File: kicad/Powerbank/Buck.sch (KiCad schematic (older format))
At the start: 1 part

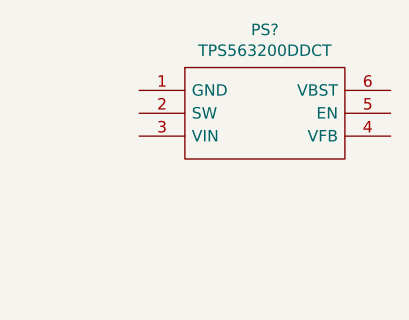
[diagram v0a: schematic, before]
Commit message: Battery charger completed according to reference guide
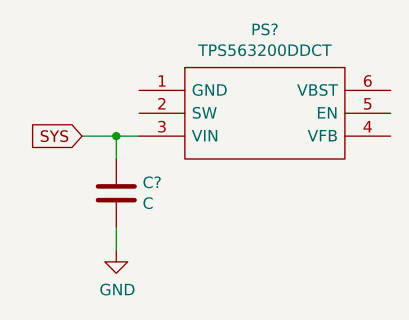
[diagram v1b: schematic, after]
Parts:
- added C?: C, symbol Device:C
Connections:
- net SYS: now reaches PS?.3 (VIN)
- net SYS: now also C?.1
- new net GND: C?.2
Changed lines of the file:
@@
 	1    0    0    -1
 $EndComp
+Text GLabel 4700 4050 0    50   Input ~ 0
+SYS
+Wire Wire Line
+	4700 4050 4850 4050
+$Comp
+L Device:C C?
+U 1 1 5E70F357
+P 4850 4300
+F 0 "C?" H 4965 4346 50  0000 L CNN
+F 1 "C" H 4965 4255 50  0000 L CNN
+F 2 "" H 4888 4150 50  0001 C CNN
+F 3 "~" H 4850 4300 50  0001 C CNN
+	1    4850 4300
+	1    0    0    -1
+$EndComp
+Wire Wire Line
+	4850 4150 4850 4050
+Connection ~ 4850 4050
+Wire Wire Line
+	4850 4050 4950 4050
+$Comp
+L power:GND #PWR?
+U 1 1 5E70FB38
+P 4850 4550
+F 0 "#PWR?" H 4850 4300 50  0001 C CNN
+F 1 "GND" H 4855 4377 50  0000 C CNN
+F 2 "" H 4850 4550 50  0001 C CNN
+F 3 "" H 4850 4550 50  0001 C CNN
+	1    4850 4550
+	1    0    0    -1
+$EndComp
+Wire Wire Line
+	4850 4550 4850 4450
 $EndSCHEMATC

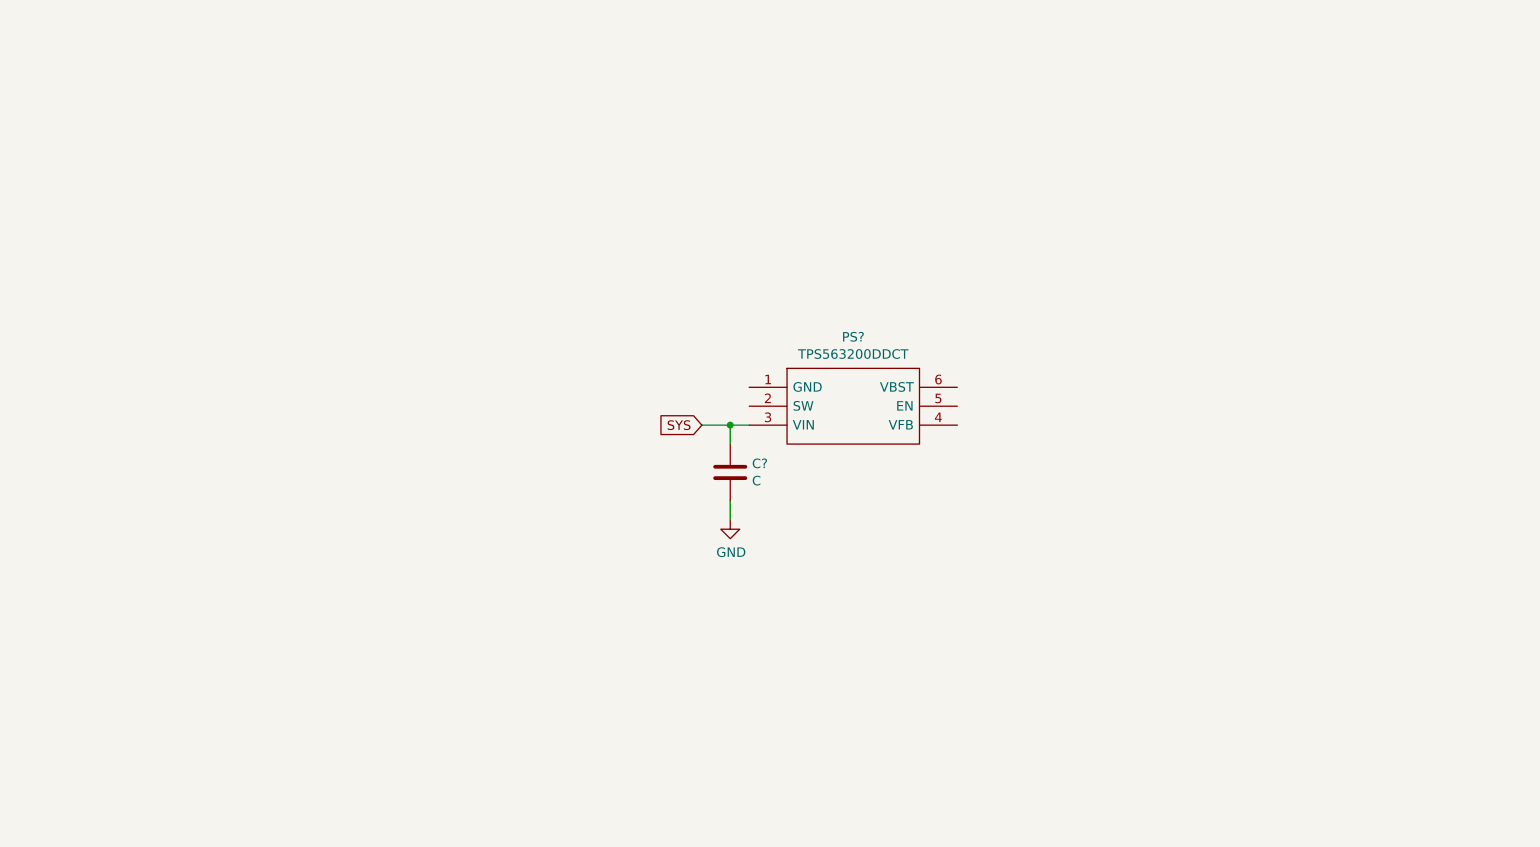
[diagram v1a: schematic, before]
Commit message: Completed buck according to reference guide
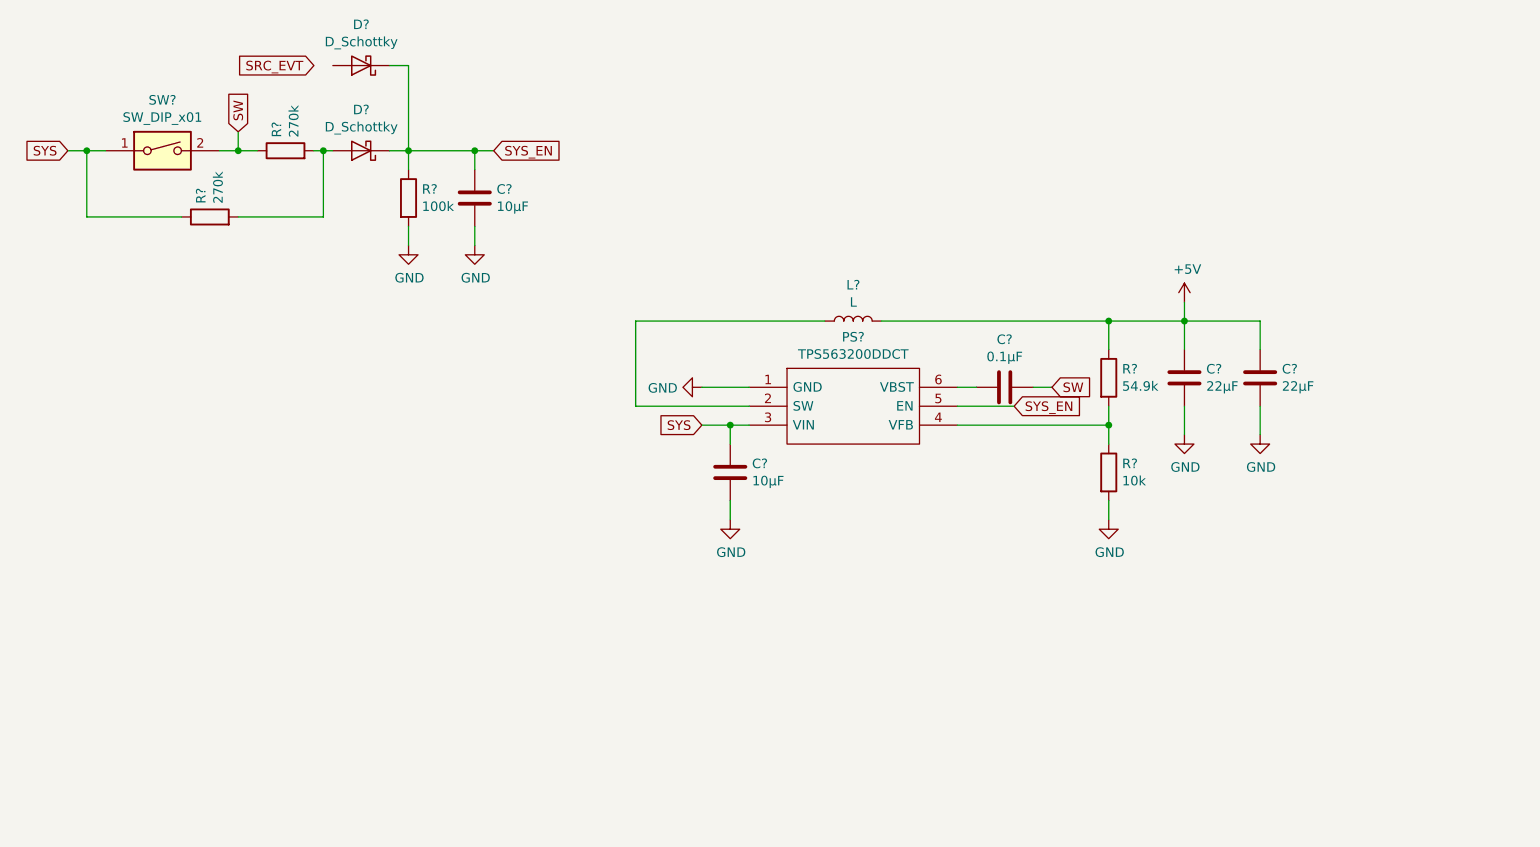
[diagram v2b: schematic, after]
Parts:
- added C?: 0.1µF, symbol Device:C
- added C? (x2): 22µF, symbol Device:C
- added C?: 10µF, symbol Device:C
- added D? (x2): D_Schottky, symbol Device:D_Schottky
- added L?: L, symbol Device:L
- added R?: 54.9k, symbol Device:R
- added R?: 10k, symbol Device:R
- added R?: 100k, symbol Device:R
- added R? (x2): 270k, symbol Device:R
- added SW?: SW_DIP_x01, symbol Switch:SW_DIP_x01
- C?: value C -> 10µF
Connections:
- net GND: now also PS?.1 (GND), C?.1, C?.2, C?.2, R?.2, R?.2
- net SYS: now also R?.1, SW?.1
- net at PS?.2 (SW): now also L?.1
- net at PS?.4 (VFB): now also R?.1, R?.2
- net SYS_EN: now reaches PS?.5 (EN)
- net SYS_EN: now also C?.2, D?.1 (K), D?.1 (K), R?.1
- net at PS?.6 (VBST): now also C?.2
- new net: D?.2 (A), R?.2, R?.2
- new net +5V: C?.1, C?.1, L?.2, R?.1
- new net SW: C?.1, R?.1, SW?.2

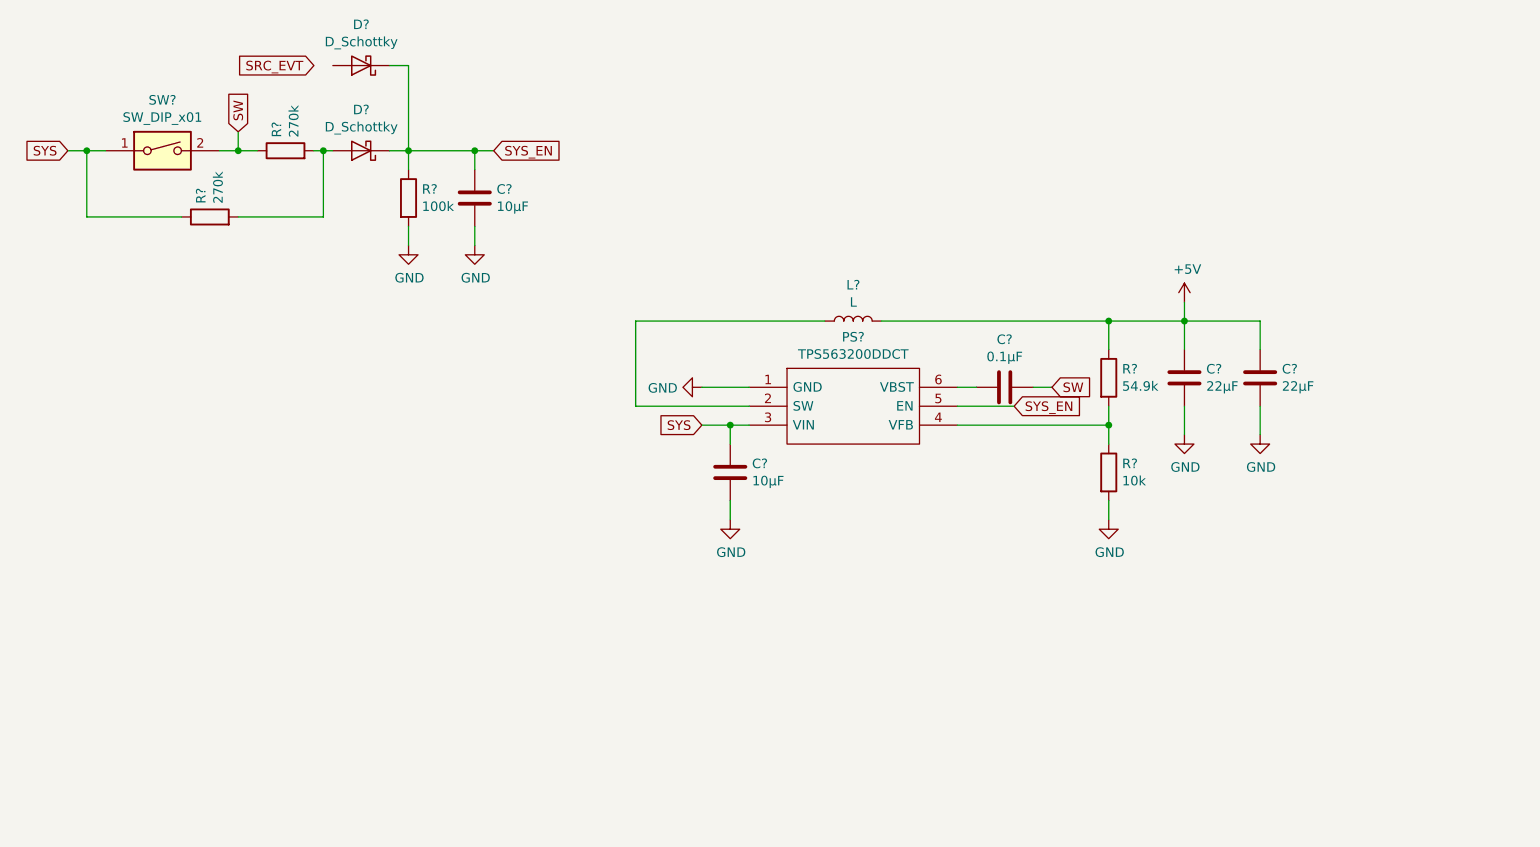
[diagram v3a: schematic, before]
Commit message: Moved LDO to Buck sheet and started check of components
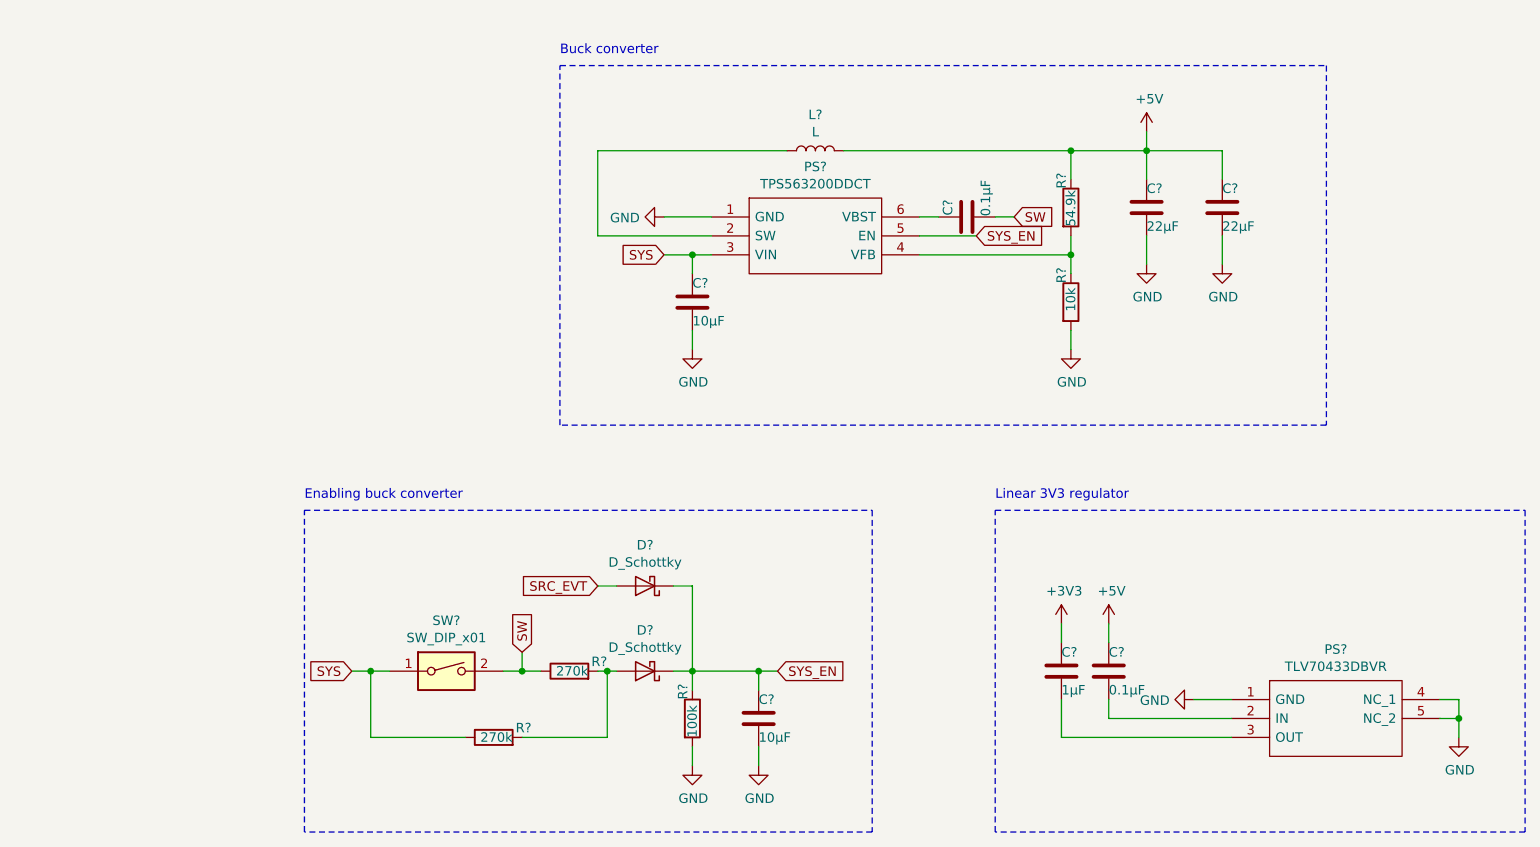
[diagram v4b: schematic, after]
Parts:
- added C?: 0.1µF, symbol Device:C
- added C?: 1µF, symbol Device:C
- added PS?: TLV70433DBVR, SOT95P280X145-5N, symbol Powerbank:TLV70433DBVR
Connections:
- net +5V: now also C?.2
- net GND: now also PS?.1 (GND), PS?.4 (NC_1), PS?.5 (NC_2)
- net SRC_EVT: now also D?.2 (A)
- new net: C?.1, PS?.2 (IN)
- new net: C?.1, PS?.3 (OUT)
- new net +3V3: C?.2
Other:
- note added: "Buck converter"
- note added: "Enabling buck converter"
- note added: "Linear 3V3 regulator"
- moved on the sheet: C?, D?, L?, PS?, R?, SW?

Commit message: Updated for PCB
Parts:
- C42, C43, C44, C45, C46: renamed from C?; footprint (none) -> Capacitor_SMD:C_0603_1608Metric
- C47, C48: renamed from C?; footprint (none) -> Capacitor_SMD:C_0805_2012Metric
- L2: renamed from L?; value L -> 3.3µH
- PS1: renamed from PS?; footprint SOT95P280X110-6N -> Powerbank:SOT95P280X110-6N
- PS2: renamed from PS?; footprint SOT95P280X145-5N -> Powerbank:SOT95P280X145-5N
- R52, R53, R54, R55, R56: renamed from R?; footprint (none) -> Resistor_SMD:R_0603_1608Metric
- gave numbers to parts that had none: 3
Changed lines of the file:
@@
 EESchema Schematic File Version 4
+LIBS:Powerbank-cache
 EELAYER 30 0
 EELAYER END
@@
 $EndDescr
 $Comp
-L Powerbank:TPS563200DDCT PS?
+L Powerbank:TPS563200DDCT PS1
 U 1 1 5E0D0DE8
 P 4750 2950
-F 0 "PS?" H 5300 3215 50  0000 C CNN
+F 0 "PS1" H 5300 3215 50  0000 C CNN
 F 1 "TPS563200DDCT" H 5300 3124 50  0000 C CNN
-F 2 "SOT95P280X110-6N" H 5700 3050 50  0001 L CNN
+F 2 "Powerbank:SOT95P280X110-6N" H 5700 3050 50  0001 L CNN
 F 3 "http://www.ti.com/lit/gpn/tps563200" H 5700 2950 50  0001 L CNN
 F 4 "Texas Instruments, TPS563200DDCT DC-DC Converter 2A Adjustable, 0.76  7 V, 6-Pin SOT-23" H 5700 2850 50  0001 L CNN "Description"
@@
 	4500 3150 4650 3150
 $Comp
-L Device:C C?
+L Device:C C42
 U 1 1 5E70F357
 P 4650 3400
-F 0 "C?" H 4650 3500 50  0000 L CNN
+F 0 "C42" H 4650 3500 50  0000 L CNN
 F 1 "10µF" H 4650 3300 50  0000 L CNN
-F 2 "" H 4688 3250 50  0001 C CNN
+F 2 "Capacitor_SMD:C_0603_1608Metric" H 4688 3250 50  0001 C CNN
 F 3 "~" H 4650 3400 50  0001 C CNN
 	1    4650 3400
@@
 	6150 3050 5850 3050
 $Comp
-L Device:C C?
+L Device:C C44
 U 1 1 5E712B04
 P 6100 2950
-F 0 "C?" H 6050 2850 50  0000 C CNN
+F 0 "C44" H 6050 2850 50  0000 C CNN
 F 1 "0.1µF" H 6000 3050 50  0000 C CNN
-F 2 "" H 6138 2800 50  0001 C CNN
+F 2 "Capacitor_SMD:C_0603_1608Metric" H 6138 2800 50  0001 C CNN
 F 3 "~" H 6100 2950 50  0001 C CNN
 	1    6100 2950
@@
 	4150 3050 4750 3050
 $Comp
-L Device:L L?
+L Device:L L2
 U 1 1 5E71971D
 P 5300 2600
-F 0 "L?" V 5490 2600 50  0000 C CNN
-F 1 "L" V 5399 2600 50  0000 C CNN
+F 0 "L2" V 5490 2600 50  0000 C CNN
+F 1 "3.3µH" V 5399 2600 50  0000 C CNN
 F 2 "" H 5300 2600 50  0001 C CNN
 F 3 "~" H 5300 2600 50  0001 C CNN
@@
 $EndComp
 $Comp
-L Device:R R?
+L Device:R R55
 U 1 1 5E71B0B1
 P 6650 2900
-F 0 "R?" V 6600 3000 50  0000 L CNN
+F 0 "R55" V 6600 3000 50  0000 L CNN
 F 1 "54.9k" V 6650 2800 50  0000 L CNN
-F 2 "" V 6580 2900 50  0001 C CNN
+F 2 "Resistor_SMD:R_0603_1608Metric" V 6580 2900 50  0001 C CNN
 F 3 "~" H 6650 2900 50  0001 C CNN
 	1    6650 2900
@@
 $EndComp
 $Comp
-L Device:R R?
+L Device:R R56
 U 1 1 5E71B6A6
 P 6650 3400
-F 0 "R?" V 6600 3500 50  0000 L CNN
+F 0 "R56" V 6600 3500 50  0000 L CNN
 F 1 "10k" V 6650 3350 50  0000 L CNN
-F 2 "" V 6580 3400 50  0001 C CNN
+F 2 "Resistor_SMD:R_0603_1608Metric" V 6580 3400 50  0001 C CNN
 F 3 "~" H 6650 3400 50  0001 C CNN
 	1    6650 3400
@@
 	5450 2600 6650 2600
 $Comp
-L Device:C C?
+L Device:C C47
 U 1 1 5E71E749
 P 7050 2900
-F 0 "C?" H 7050 3000 50  0000 L CNN
+F 0 "C47" H 7050 3000 50  0000 L CNN
 F 1 "22µF" H 7050 2800 50  0000 L CNN
-F 2 "" H 7088 2750 50  0001 C CNN
+F 2 "Capacitor_SMD:C_0805_2012Metric" H 7088 2750 50  0001 C CNN
 F 3 "~" H 7050 2900 50  0001 C CNN
 	1    7050 2900
@@
 $EndComp
 $Comp
-L Device:C C?
+L Device:C C48
 U 1 1 5E71EA49
 P 7450 2900
-F 0 "C?" H 7450 3000 50  0000 L CNN
+F 0 "C48" H 7450 3000 50  0000 L CNN
 F 1 "22µF" H 7450 2800 50  0000 L CNN
-F 2 "" H 7488 2750 50  0001 C CNN
+F 2 "Capacitor_SMD:C_0805_2012Metric" H 7488 2750 50  0001 C CNN
 F 3 "~" H 7450 2900 50  0001 C CNN
 	1    7450 2900
@@
 	7050 2500 7050 2600
 $Comp
-L Device:D_Schottky D?
+L Device:D_Schottky D8
 U 1 1 5E731DF5
 P 4400 4900
-F 0 "D?" H 4400 4684 50  0000 C CNN
+F 0 "D8" H 4400 4684 50  0000 C CNN
 F 1 "D_Schottky" H 4400 4775 50  0000 C CNN
 F 2 "" H 4400 4900 50  0001 C CNN
@@
 $EndComp
 $Comp
-L Device:D_Schottky D?
+L Device:D_Schottky D9
 U 1 1 5E732536
 P 4400 5350
-F 0 "D?" H 4400 5134 50  0000 C CNN
+F 0 "D9" H 4400 5134 50  0000 C CNN
 F 1 "D_Schottky" H 4400 5225 50  0000 C CNN
 F 2 "" H 4400 5350 50  0001 C CNN
@@
 $EndComp
 $Comp
-L Device:C C?
+L Device:C C43
 U 1 1 5E732D64
 P 5000 5600
-F 0 "C?" H 5000 5500 50  0000 R CNN
+F 0 "C43" H 5000 5500 50  0000 R CNN
 F 1 "10µF" H 5000 5700 50  0000 R CNN
-F 2 "" H 5038 5450 50  0001 C CNN
+F 2 "Capacitor_SMD:C_0603_1608Metric" H 5038 5450 50  0001 C CNN
 F 3 "~" H 5000 5600 50  0001 C CNN
 	1    5000 5600
@@
 $EndComp
 $Comp
-L Device:R R?
+L Device:R R54
 U 1 1 5E733EB3
 P 4650 5600
-F 0 "R?" V 4600 5700 50  0000 L CNN
+F 0 "R54" V 4600 5700 50  0000 L CNN
 F 1 "100k" V 4650 5500 50  0000 L CNN
-F 2 "" V 4580 5600 50  0001 C CNN
+F 2 "Resistor_SMD:R_0603_1608Metric" V 4580 5600 50  0001 C CNN
 F 3 "~" H 4650 5600 50  0001 C CNN
 	1    4650 5600
@@
 	4150 5350 4200 5350
 $Comp
-L Device:R R?
+L Device:R R53
 U 1 1 5E7390CD
 P 4000 5350
-F 0 "R?" V 4050 5150 50  0000 L CNN
+F 0 "R53" V 4050 5150 50  0000 L CNN
 F 1 "270k" V 4000 5250 50  0000 L CNN
-F 2 "" V 3930 5350 50  0001 C CNN
+F 2 "Resistor_SMD:R_0603_1608Metric" V 3930 5350 50  0001 C CNN
 F 3 "~" H 4000 5350 50  0001 C CNN
 	1    4000 5350
@@
 	3750 5350 3750 5250
 $Comp
-L Switch:SW_DIP_x01 SW?
+L Switch:SW_DIP_x01 SW1
 U 1 1 5E73AC92
 P 3350 5350
-F 0 "SW?" H 3350 5617 50  0000 C CNN
+F 0 "SW1" H 3350 5617 50  0000 C CNN
 F 1 "SW_DIP_x01" H 3350 5526 50  0000 C CNN
 F 2 "" H 3350 5350 50  0001 C CNN
@@
 Connection ~ 3750 5350
 $Comp
-L Device:R R?
+L Device:R R52
 U 1 1 5E73BA05
 P 3600 5700
-F 0 "R?" V 3650 5500 50  0000 L CNN
+F 0 "R52" V 3650 5500 50  0000 L CNN
 F 1 "270k" V 3600 5600 50  0000 L CNN
-F 2 "" V 3530 5700 50  0001 C CNN
+F 2 "Resistor_SMD:R_0603_1608Metric" V 3530 5700 50  0001 C CNN
 F 3 "~" H 3600 5700 50  0001 C CNN
 	1    3600 5700
@@
 P 7500 5500
 AR Path="/5E0D16A0/5EA14ADF" Ref="PS?"  Part="1"
-AR Path="/5E0D0913/5EA14ADF" Ref="PS?"  Part="1"
-F 0 "PS?" H 8050 5765 50  0000 C CNN
+AR Path="/5E0D0913/5EA14ADF" Ref="PS2"  Part="1"
+F 0 "PS2" H 8050 5765 50  0000 C CNN
 F 1 "TLV70433DBVR" H 8050 5674 50  0000 C CNN
-F 2 "SOT95P280X145-5N" H 8450 5600 50  0001 L CNN
+F 2 "Powerbank:SOT95P280X145-5N" H 8450 5600 50  0001 L CNN
 F 3 "http://www.ti.com/lit/gpn/tlv704" H 8450 5500 50  0001 L CNN
 F 4 "24V Input Voltage, 150mA, Ultra-Low-Iq Low-Dropout (LDO) Regulators" H 8450 5400 50  0001 L CNN "Description"
@@
 $EndComp
 $Comp
-L Device:C C?
+L Device:C C46
 U 1 1 5EA14B03
 P 6850 5350
-AR Path="/5E0D0913/5EA14B03" Ref="C?"  Part="1"
+AR Path="/5E0D0913/5EA14B03" Ref="C46"  Part="1"
 AR Path="/5E0D16A0/5EA14B03" Ref="C?"  Part="1"
-F 0 "C?" H 6850 5250 50  0000 R CNN
+F 0 "C46" H 6850 5250 50  0000 R CNN
 F 1 "0.1µF" H 6850 5450 50  0000 R CNN
-F 2 "" H 6888 5200 50  0001 C CNN
+F 2 "Capacitor_SMD:C_0603_1608Metric" H 6888 5200 50  0001 C CNN
 F 3 "~" H 6850 5350 50  0001 C CNN
 	1    6850 5350
@@
 	6850 5600 7500 5600
 $Comp
-L Device:C C?
+L Device:C C45
 U 1 1 5EA14B0C
 P 6600 5350
-AR Path="/5E0D0913/5EA14B0C" Ref="C?"  Part="1"
+AR Path="/5E0D0913/5EA14B0C" Ref="C45"  Part="1"
 AR Path="/5E0D16A0/5EA14B0C" Ref="C?"  Part="1"
-F 0 "C?" H 6600 5250 50  0000 R CNN
+F 0 "C45" H 6600 5250 50  0000 R CNN
 F 1 "1µF" H 6600 5450 50  0000 R CNN
-F 2 "" H 6638 5200 50  0001 C CNN
+F 2 "Capacitor_SMD:C_0603_1608Metric" H 6638 5200 50  0001 C CNN
 F 3 "~" H 6600 5350 50  0001 C CNN
 	1    6600 5350

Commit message: Assigned inductor with footprint
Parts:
- L2: footprint (none) -> Powerbank:WE_Inductor_8070_7443340330
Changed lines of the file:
@@
 F 0 "L2" V 5490 2600 50  0000 C CNN
 F 1 "3.3µH" V 5399 2600 50  0000 C CNN
-F 2 "" H 5300 2600 50  0001 C CNN
+F 2 "Powerbank:WE_Inductor_8070_7443340330" H 5300 2600 50  0001 C CNN
 F 3 "~" H 5300 2600 50  0001 C CNN
 	1    5300 2600

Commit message: Added footprint for all, moved to a first attempt for routing
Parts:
- D8, D9: footprint (none) -> Diode_SMD:D_SOD-523
- SW1: footprint (none) -> Powerbank:SW_B3U-3000P
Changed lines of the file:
@@
 F 0 "D8" H 4400 4684 50  0000 C CNN
 F 1 "D_Schottky" H 4400 4775 50  0000 C CNN
-F 2 "" H 4400 4900 50  0001 C CNN
+F 2 "Diode_SMD:D_SOD-523" H 4400 4900 50  0001 C CNN
 F 3 "~" H 4400 4900 50  0001 C CNN
 	1    4400 4900
@@
 F 0 "D9" H 4400 5134 50  0000 C CNN
 F 1 "D_Schottky" H 4400 5225 50  0000 C CNN
-F 2 "" H 4400 5350 50  0001 C CNN
+F 2 "Diode_SMD:D_SOD-523" H 4400 5350 50  0001 C CNN
 F 3 "~" H 4400 5350 50  0001 C CNN
 	1    4400 5350
@@
 F 0 "SW1" H 3350 5617 50  0000 C CNN
 F 1 "SW_DIP_x01" H 3350 5526 50  0000 C CNN
-F 2 "" H 3350 5350 50  0001 C CNN
+F 2 "Powerbank:SW_B3U-3000P" H 3350 5350 50  0001 C CNN
 F 3 "~" H 3350 5350 50  0001 C CNN
 	1    3350 5350
